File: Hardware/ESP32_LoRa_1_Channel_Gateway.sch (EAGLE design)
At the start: 40 parts, among them J1 USB, J2 U.FL, J6 QWIIC, Q1 MBT3904DW1T1, U1 3.3V, U2 ESP-WROOM-32NARROW, U3 CH340C, U4 RFM95W

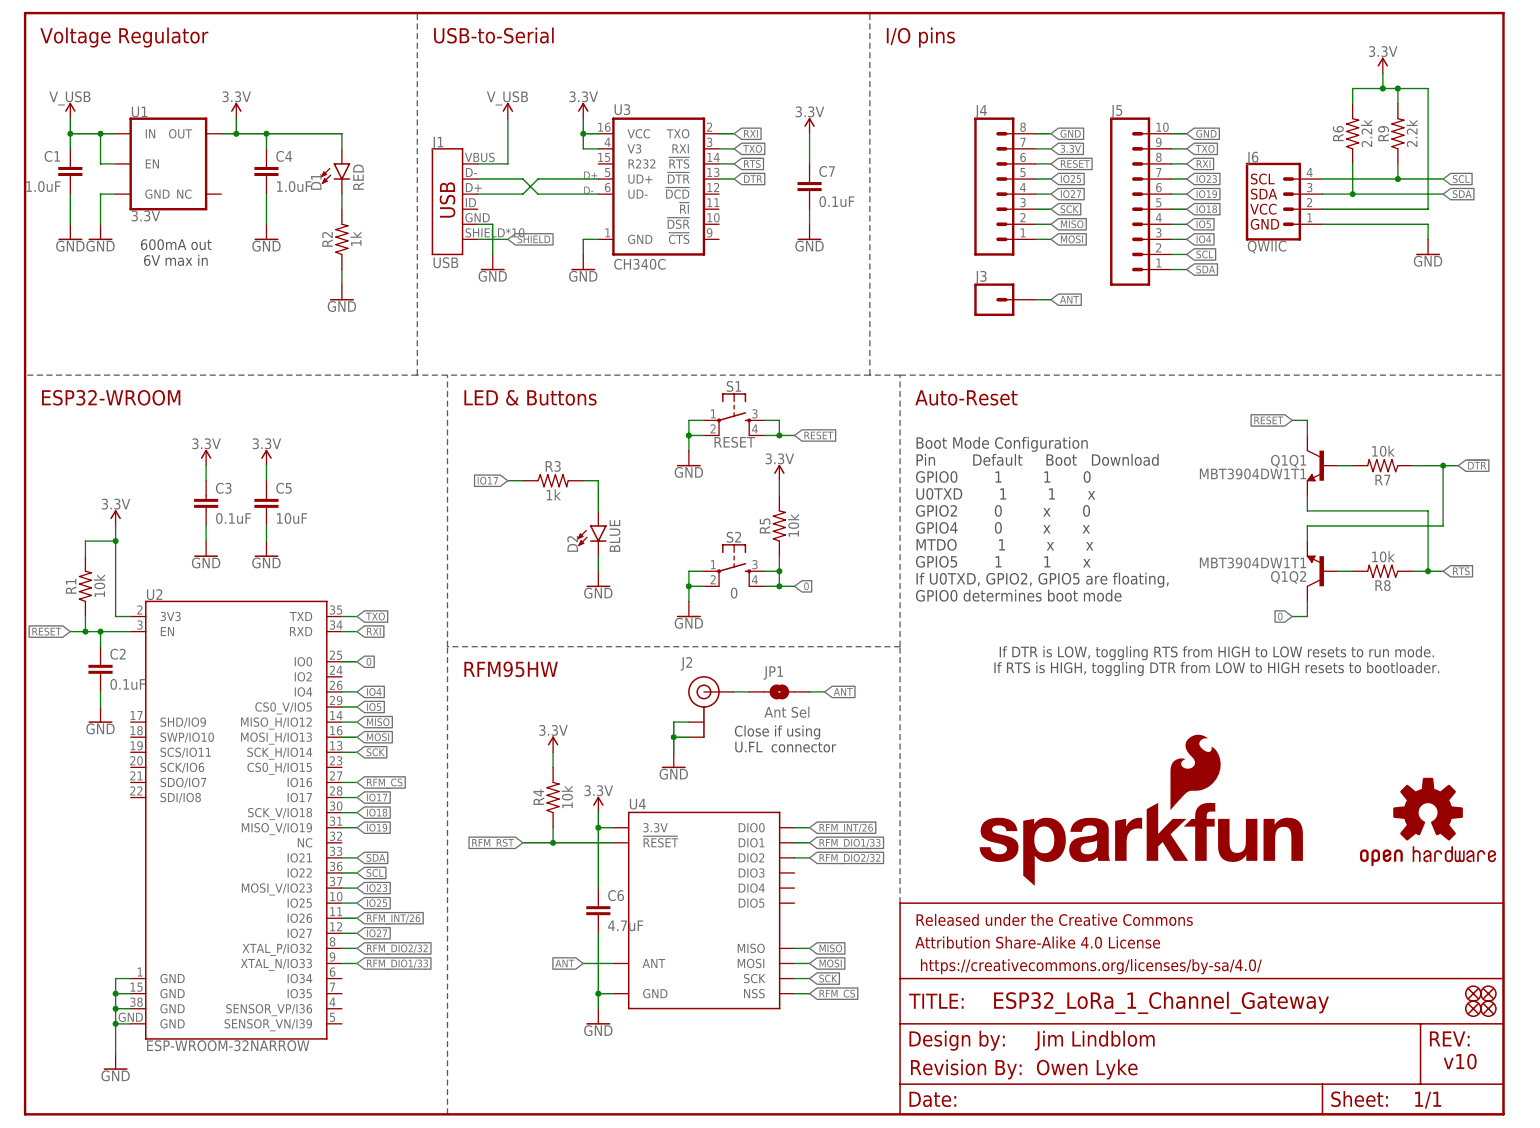
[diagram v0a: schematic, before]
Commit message: Updated Momentary Switches
Updated Switches from SWCH-13065 to SWCH-15606
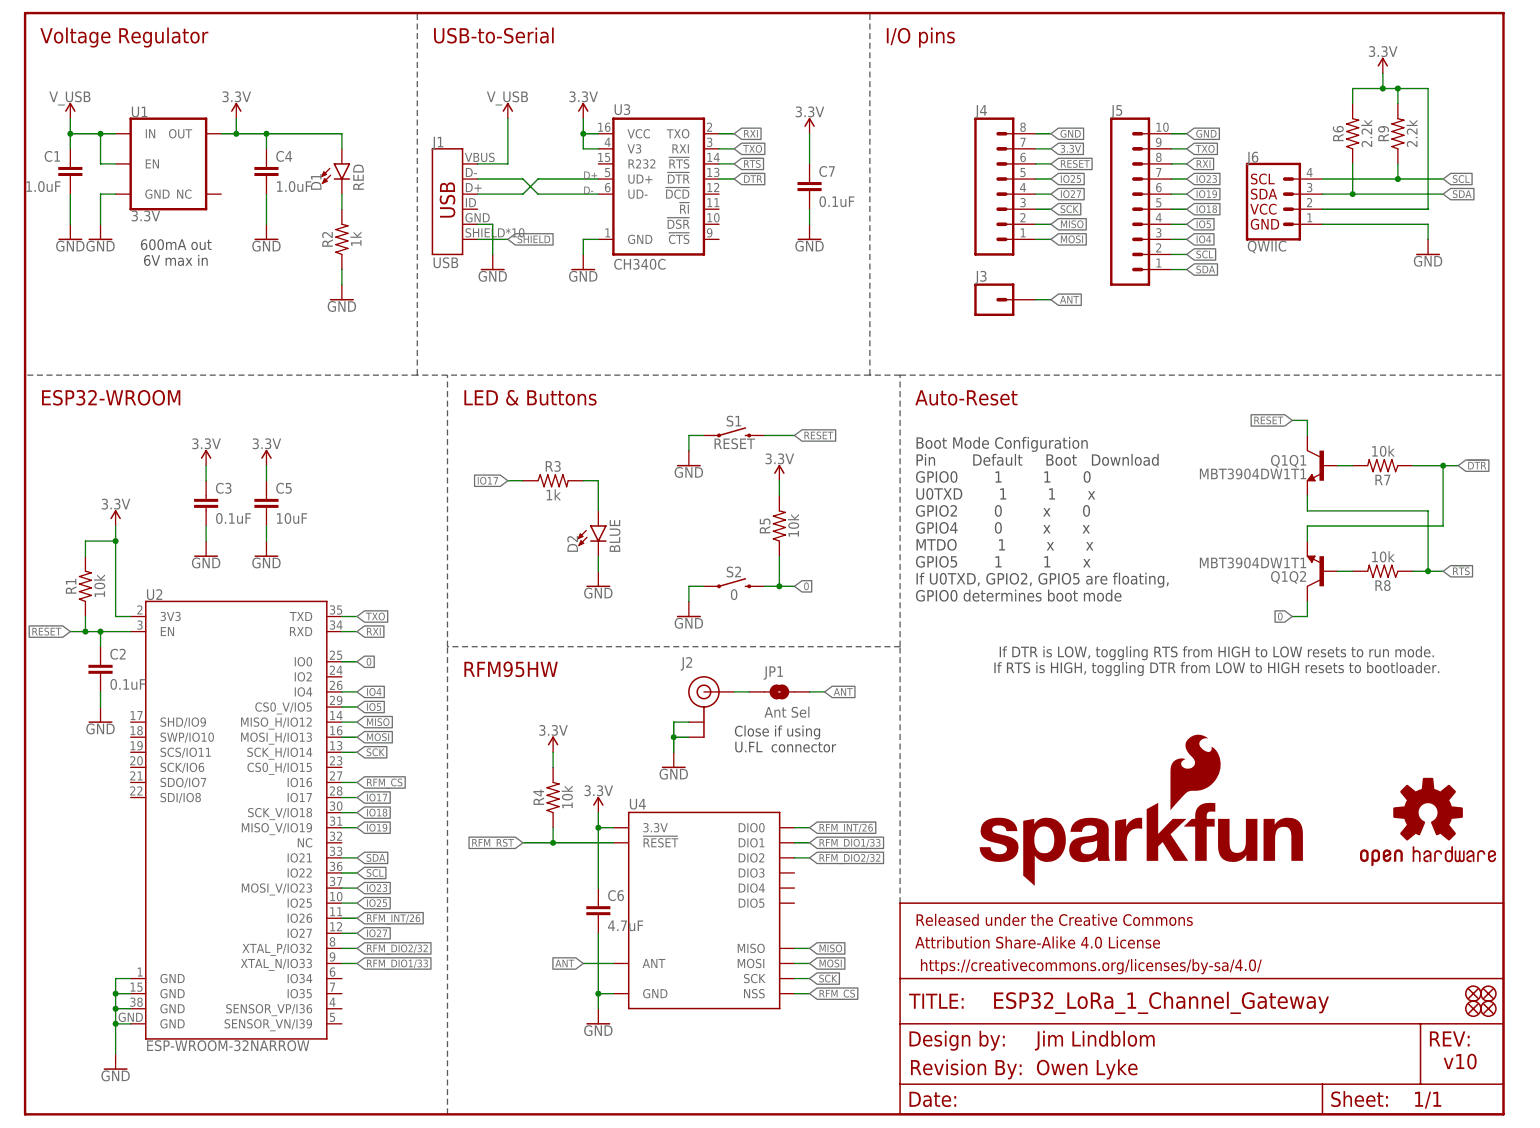
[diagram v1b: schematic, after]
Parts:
- S1, S2: device SparkFun-Switches:MOMENTARY-SWITCH-SPST-2-SMD-4.6X2.8MM -> SparkFun-Switches:MOMENTARY-SWITCH-SPST-SMD-4.6X2.8MM
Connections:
- net 0: now also S2.2; no longer S2.3, S2.4
- net GND: no longer S1.2, S2.2
- net RESET: now also S1.2; no longer S1.3, S1.4
